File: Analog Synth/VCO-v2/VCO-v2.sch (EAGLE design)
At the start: 127 parts, among them IC1 TL084P, IC2 TL084P, IC3 78L09, IC4 78L05, IC5 79L09\, IC6 79L05, IC7 TL084P, Q1 J310, Q2 J310, Q3 2N3904, Q4 2N3904, Q5 2N3904, Q6 2N3906, T1 2N3904, T2 2N3904, T3 2N3904, T4 2N3904, T7 2N3904, U1 CA3096

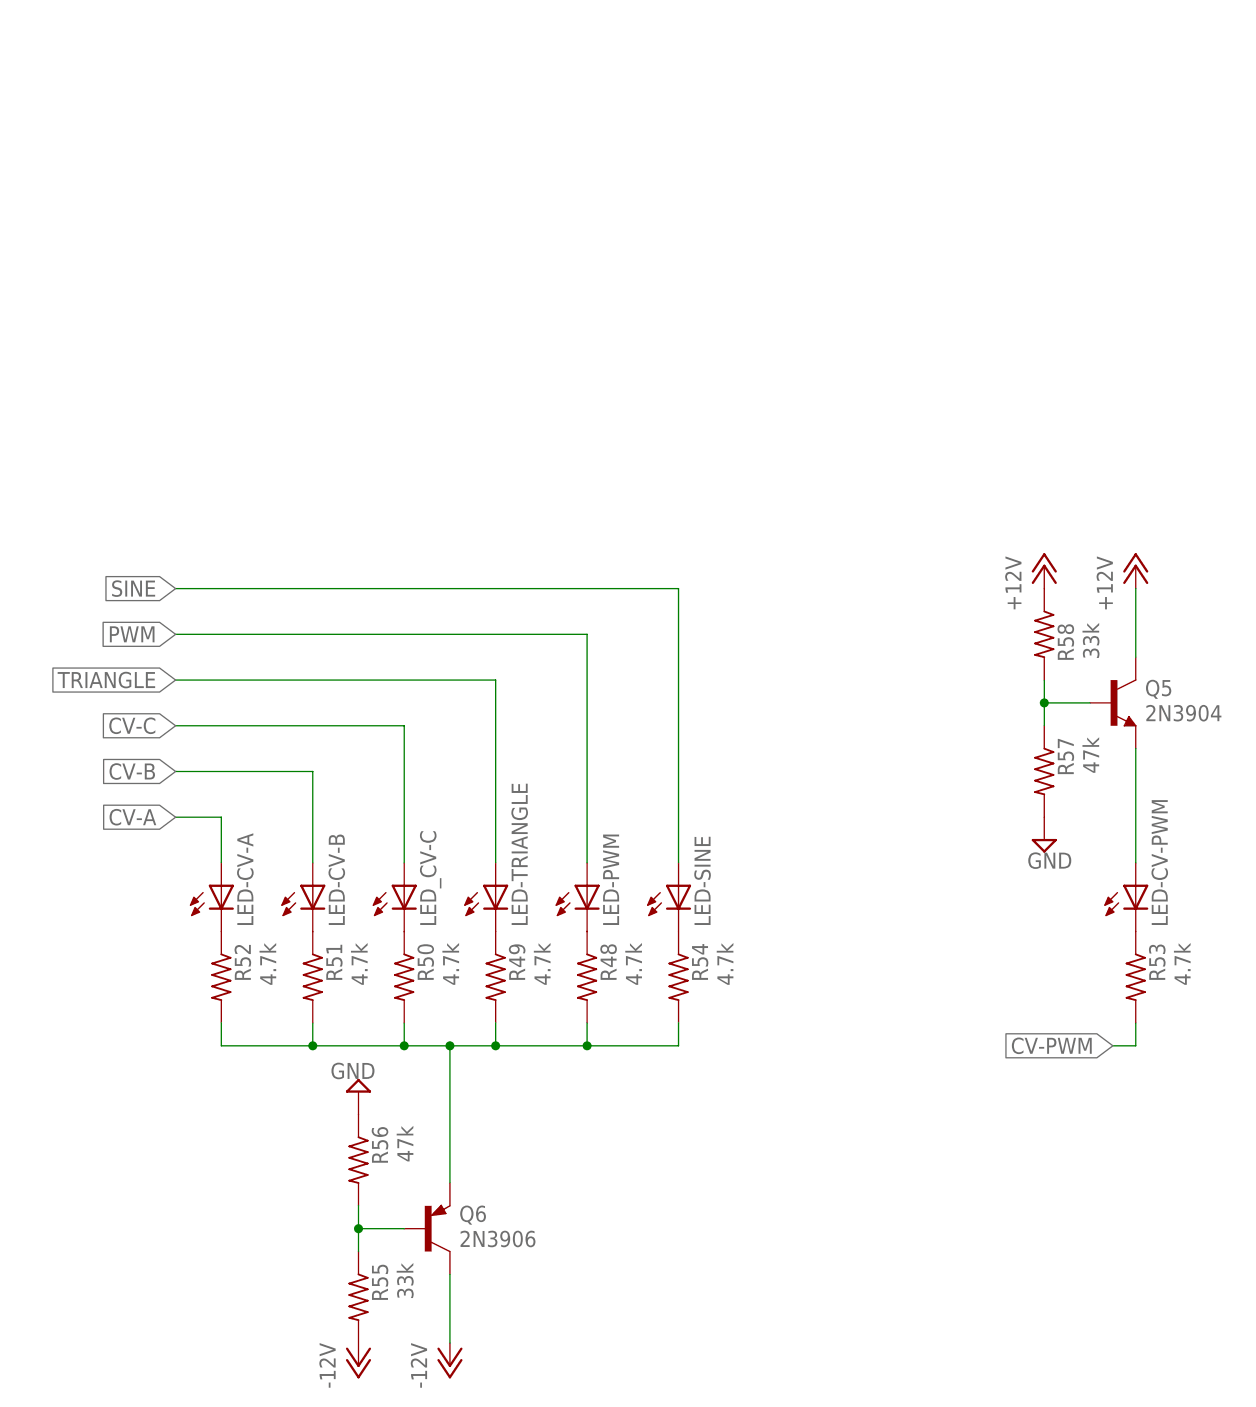
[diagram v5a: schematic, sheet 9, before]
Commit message: VCO-v2 improved readability
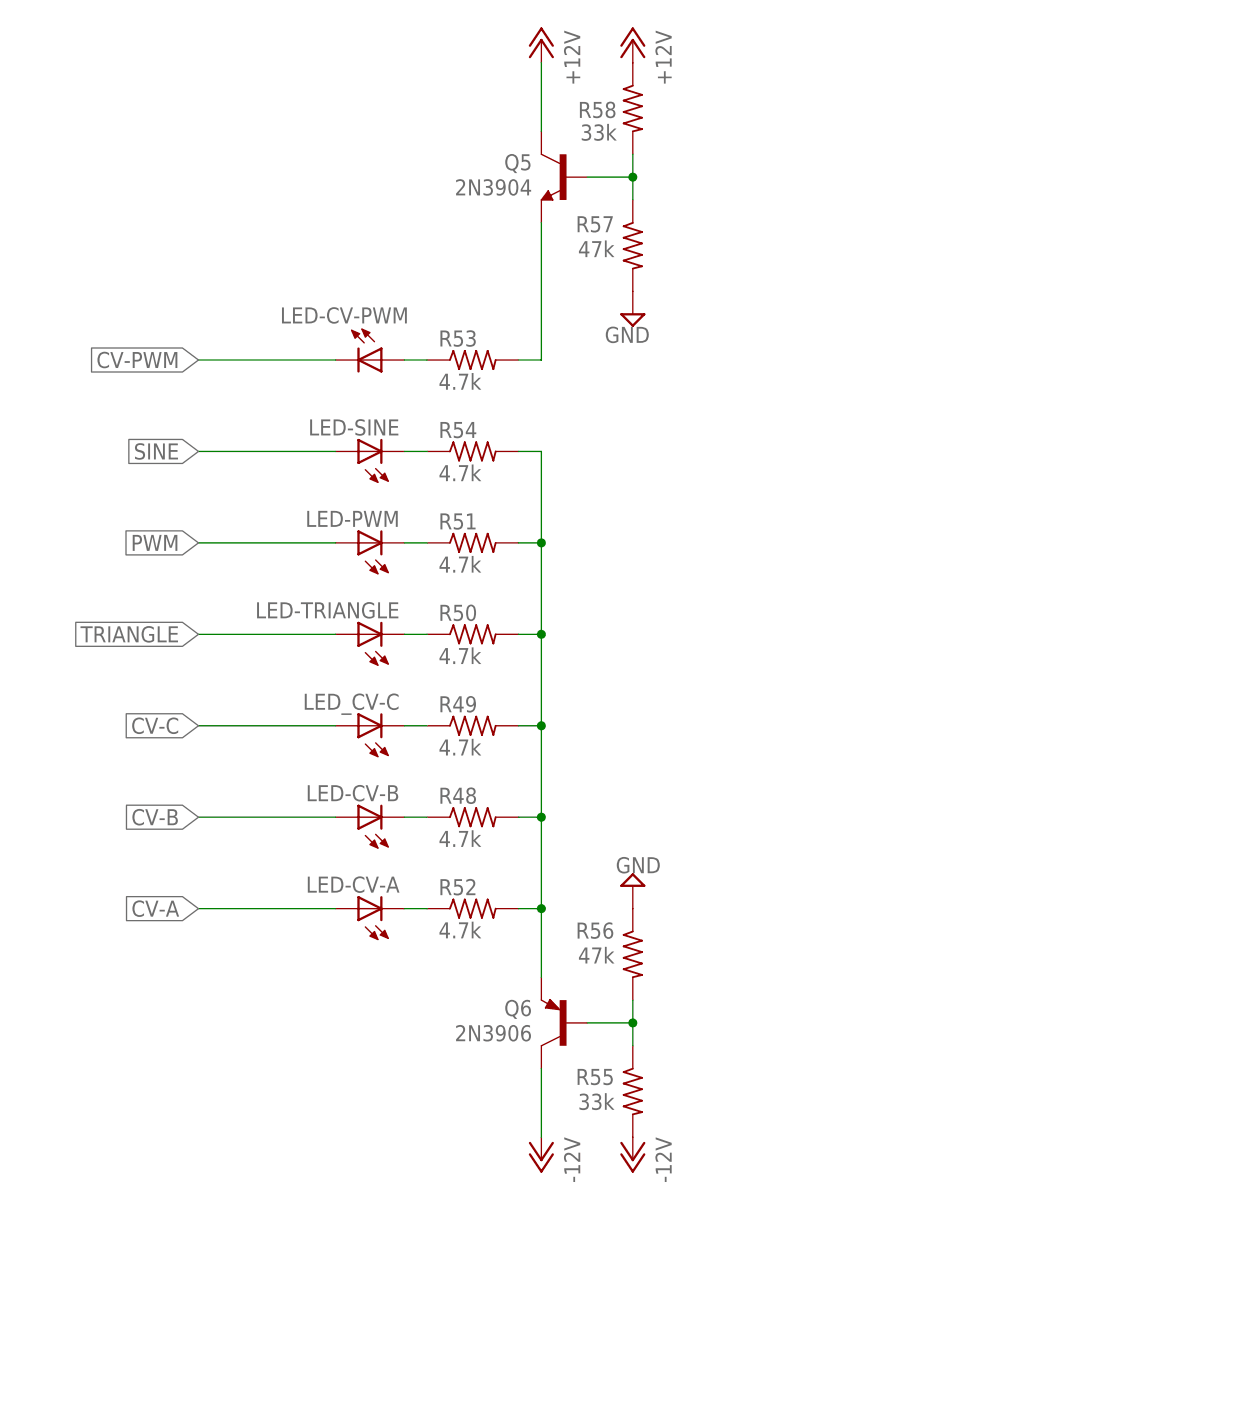
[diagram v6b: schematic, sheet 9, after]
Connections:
- removed net N$36 (its old number): C21.1
- removed net N$57: LED_CV-C.C, R50.1
- removed net N$58: LED-CV-PWM.A, Q5.E
- removed net N$59: LED-PWM.C, R48.1
- removed net N$60: LED-TRIANGLE.C, R49.1
- new net N$61: LED_CV-C.C, R49.1
- new net N$62: LED-TRIANGLE.C, R50.1
- new net N$63: LED-PWM.C, R51.1
- new net N$7: LED-CV-PWM.A, R53.1
- net -12V: now also C10.-; no longer C10.+
- net -5V: now also C16.-, C21.1; no longer C16.+
- net -9V: now also C13.-; no longer C13.+
- net CV-PWM: now also LED-CV-PWM.C; no longer R53.2
- net GND: now also C10.+, C13.+, C16.+; no longer C10.-, C13.-, C16.-
- net N$11: now also Q5.E, R53.2; no longer LED-CV-PWM.C, R53.1
- net N$56: now also R48.1; no longer R51.1
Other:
- moved on the sheet: C10, C13, C16, HIGH-FREQ, LED-CV-A, LED-CV-B, LED-CV-PWM, LED-PWM, LED-SINE, LED-TRIANGLE, LED_CV-C, Q5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

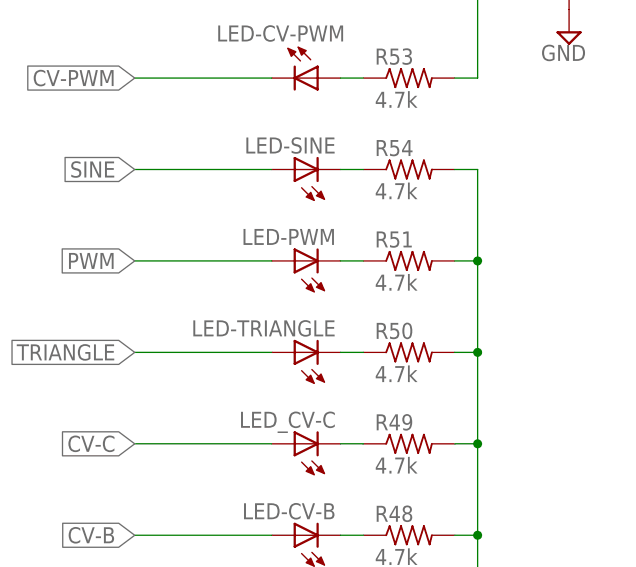
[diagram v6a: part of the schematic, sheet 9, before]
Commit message: VCO-v2.2 - updated an LED resistor value and exported PDF
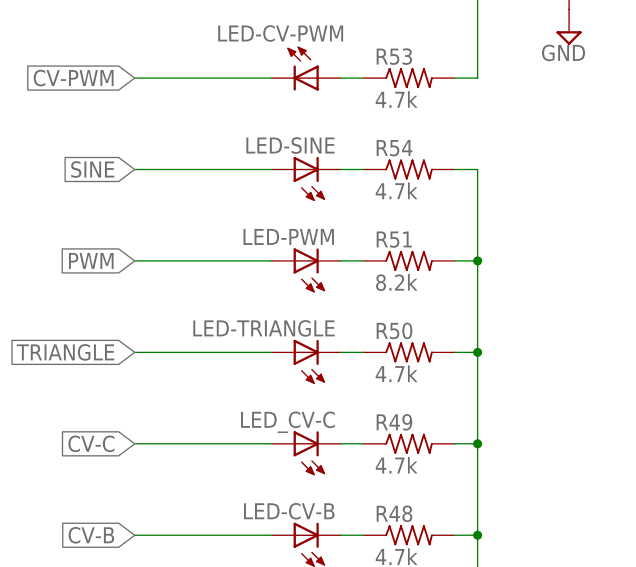
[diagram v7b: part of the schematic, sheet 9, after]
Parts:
- R51: value 4.7k -> 8.2k
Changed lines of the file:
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@@
 <grid distance="0.1" unitdist="inch" unit="inch" style="lines" multiple="1" display="no" altdistance="0.01" altunitdist="inch" altunit="inch"/>
 <layers>
-<layer number="1" name="Top" color="4" fill="1" visible="yes" active="no"/>
-<layer number="2" name="Route2" color="1" fill="3" visible="yes" active="no"/>
-<layer number="3" name="Route3" color="4" fill="3" visible="yes" active="no"/>
-<layer number="4" name="Route4" color="1" fill="4" visible="yes" active="no"/>
-<layer number="5" name="Route5" color="4" fill="4" visible="yes" active="no"/>
-<layer number="6" name="Route6" color="1" fill="8" visible="yes" active="no"/>
-<layer number="7" name="Route7" color="4" fill="8" visible="yes" active="no"/>
-<layer number="8" name="Route8" color="1" fill="2" visible="yes" active="no"/>
-<layer number="9" name="Route9" color="4" fill="2" visible="yes" active="no"/>
-<layer number="10" name="Route10" color="1" fill="7" visible="yes" active="no"/>
-<layer number="11" name="Route11" color="4" fill="7" visible="yes" active="no"/>
-<layer number="12" name="Route12" color="1" fill="5" visible="yes" active="no"/>
-<layer number="13" name="Route13" color="4" fill="5" visible="yes" active="no"/>
-<layer number="14" name="Route14" color="1" fill="6" visible="yes" active="no"/>
-<layer number="15" name="Route15" color="4" fill="6" visible="yes" active="no"/>
-<layer number="16" name="Bottom" color="1" fill="1" visible="yes" active="no"/>
-<layer number="17" name="Pads" color="2" fill="1" visible="yes" active="no"/>
-<layer number="18" name="Vias" color="2" fill="1" visible="yes" active="no"/>
-<layer number="19" name="Unrouted" color="6" fill="1" visible="yes" active="no"/>
-<layer number="20" name="Dimension" color="15" fill="1" visible="yes" active="no"/>
-<layer number="21" name="tPlace" color="7" fill="1" visible="yes" active="no"/>
-<layer number="22" name="bPlace" color="7" fill="1" visible="yes" active="no"/>
-<layer number="23" name="tOrigins" color="15" fill="1" visible="yes" active="no"/>
-<layer number="24" name="bOrigins" color="15" fill="1" visible="yes" active="no"/>
-<layer number="25" name="tNames" color="7" fill="1" visible="yes" active="no"/>
-<layer number="26" name="bNames" color="7" fill="1" visible="yes" active="no"/>
-<layer number="27" name="tValues" color="7" fill="1" visible="yes" active="no"/>
-<layer number="28" name="bValues" color="7" fill="1" visible="yes" active="no"/>
+<layer number="1" name="Top" color="4" fill="1" visible="no" active="no"/>
+<layer number="2" name="Route2" color="1" fill="3" visible="no" active="no"/>
+<layer number="3" name="Route3" color="4" fill="3" visible="no" active="no"/>
+<layer number="4" name="Route4" color="1" fill="4" visible="no" active="no"/>
+<layer number="5" name="Route5" color="4" fill="4" visible="no" active="no"/>
+<layer number="6" name="Route6" color="1" fill="8" visible="no" active="no"/>
+<layer number="7" name="Route7" color="4" fill="8" visible="no" active="no"/>
+<layer number="8" name="Route8" color="1" fill="2" visible="no" active="no"/>
+<layer number="9" name="Route9" color="4" fill="2" visible="no" active="no"/>
+<layer number="10" name="Route10" color="1" fill="7" visible="no" active="no"/>
+<layer number="11" name="Route11" color="4" fill="7" visible="no" active="no"/>
+<layer number="12" name="Route12" color="1" fill="5" visible="no" active="no"/>
+<layer number="13" name="Route13" color="4" fill="5" visible="no" active="no"/>
+<layer number="14" name="Route14" color="1" fill="6" visible="no" active="no"/>
+<layer number="15" name="Route15" color="4" fill="6" visible="no" active="no"/>
+<layer number="16" name="Bottom" color="1" fill="1" visible="no" active="no"/>
+<layer number="17" name="Pads" color="2" fill="1" visible="no" active="no"/>
+<layer number="18" name="Vias" color="2" fill="1" visible="no" active="no"/>
+<layer number="19" name="Unrouted" color="6" fill="1" visible="no" active="no"/>
+<layer number="20" name="Dimension" color="15" fill="1" visible="no" active="no"/>
+<layer number="21" name="tPlace" color="7" fill="1" visible="no" active="no"/>
+<layer number="22" name="bPlace" color="7" fill="1" visible="no" active="no"/>
+<layer number="23" name="tOrigins" color="15" fill="1" visible="no" active="no"/>
+<layer number="24" name="bOrigins" color="15" fill="1" visible="no" active="no"/>
+<layer number="25" name="tNames" color="7" fill="1" visible="no" active="no"/>
+<layer number="26" name="bNames" color="7" fill="1" visible="no" active="no"/>
+<layer number="27" name="tValues" color="7" fill="1" visible="no" active="no"/>
+<layer number="28" name="bValues" color="7" fill="1" visible="no" active="no"/>
 <layer number="29" name="tStop" color="7" fill="3" visible="no" active="no"/>
 <layer number="30" name="bStop" color="7" fill="6" visible="no" active="no"/>
@@
 <layer number="35" name="tGlue" color="7" fill="4" visible="no" active="no"/>
 <layer number="36" name="bGlue" color="7" fill="5" visible="no" active="no"/>
-<layer number="37" name="tTest" color="7" fill="1" visible="yes" active="no"/>
-<layer number="38" name="bTest" color="7" fill="1" visible="yes" active="no"/>
+<layer number="37" name="tTest" color="7" fill="1" visible="no" active="no"/>
+<layer number="38" name="bTest" color="7" fill="1" visible="no" active="no"/>
 <layer number="39" name="tKeepout" color="4" fill="11" visible="no" active="no"/>
 <layer number="40" name="bKeepout" color="1" fill="11" visible="no" active="no"/>
@@
 <layer number="44" name="Drills" color="7" fill="1" visible="no" active="no"/>
 <layer number="45" name="Holes" color="7" fill="1" visible="no" active="no"/>
-<layer number="46" name="Milling" color="3" fill="1" visible="yes" active="no"/>
-<layer number="47" name="Measures" color="7" fill="1" visible="yes" active="no"/>
-<layer number="48" name="Document" color="7" fill="1" visible="yes" active="no"/>
-<layer number="49" name="Reference" color="7" fill="1" visible="yes" active="no"/>
-<layer number="51" name="tDocu" color="7" fill="1" visible="yes" active="no"/>
-<layer number="52" name="bDocu" color="7" fill="1" visible="yes" active="no"/>
+<layer number="46" name="Milling" color="3" fill="1" visible="no" active="no"/>
+<layer number="47" name="Measures" color="7" fill="1" visible="no" active="no"/>
+<layer number="48" name="Document" color="7" fill="1" visible="no" active="no"/>
+<layer number="49" name="Reference" color="7" fill="1" visible="no" active="no"/>
+<layer number="51" name="tDocu" color="7" fill="1" visible="no" active="no"/>
+<layer number="52" name="bDocu" color="7" fill="1" visible="no" active="no"/>
 <layer number="91" name="Nets" color="2" fill="1" visible="yes" active="yes"/>
 <layer number="92" name="Busses" color="1" fill="1" visible="yes" active="yes"/>
@@
 <part name="R49" library="resistor" deviceset="R-US_" device="0204/7" value="4.7k"/>
 <part name="R50" library="resistor" deviceset="R-US_" device="0204/7" value="4.7k"/>
-<part name="R51" library="resistor" deviceset="R-US_" device="0204/7" value="4.7k"/>
+<part name="R51" library="resistor" deviceset="R-US_" device="0204/7" value="8.2k"/>
 <part name="R54" library="resistor" deviceset="R-US_" device="0204/7" value="4.7k"/>
 <part name="R53" library="resistor" deviceset="R-US_" device="0204/7" value="4.7k"/>
